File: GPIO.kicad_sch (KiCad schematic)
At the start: 8 parts, among them IC1 ECP5-BGA256, J4 Micro_SD_Card

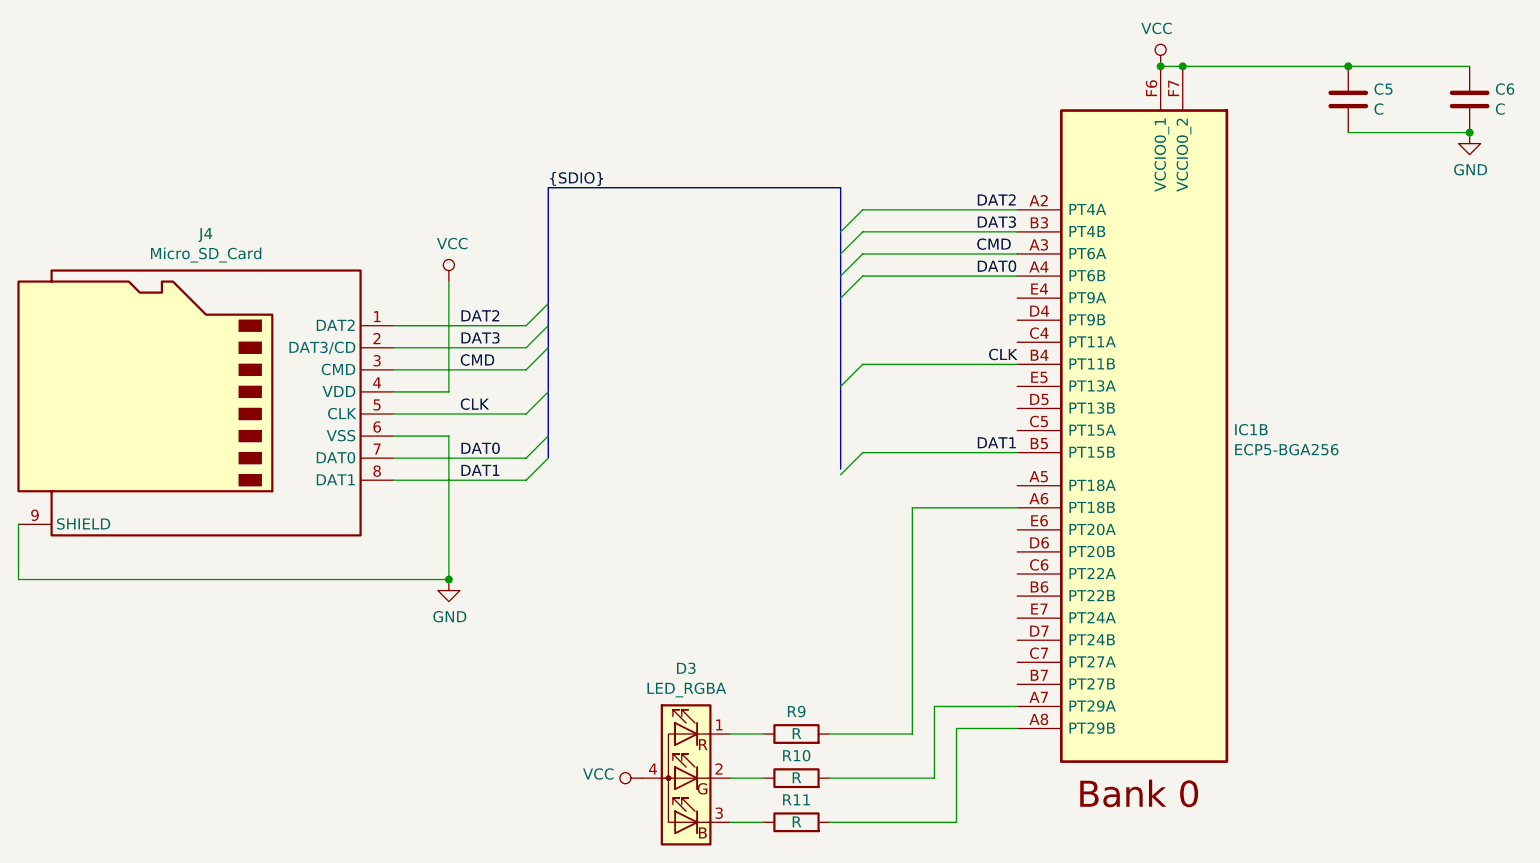
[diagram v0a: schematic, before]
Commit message: Remove SD card, relocate regulators
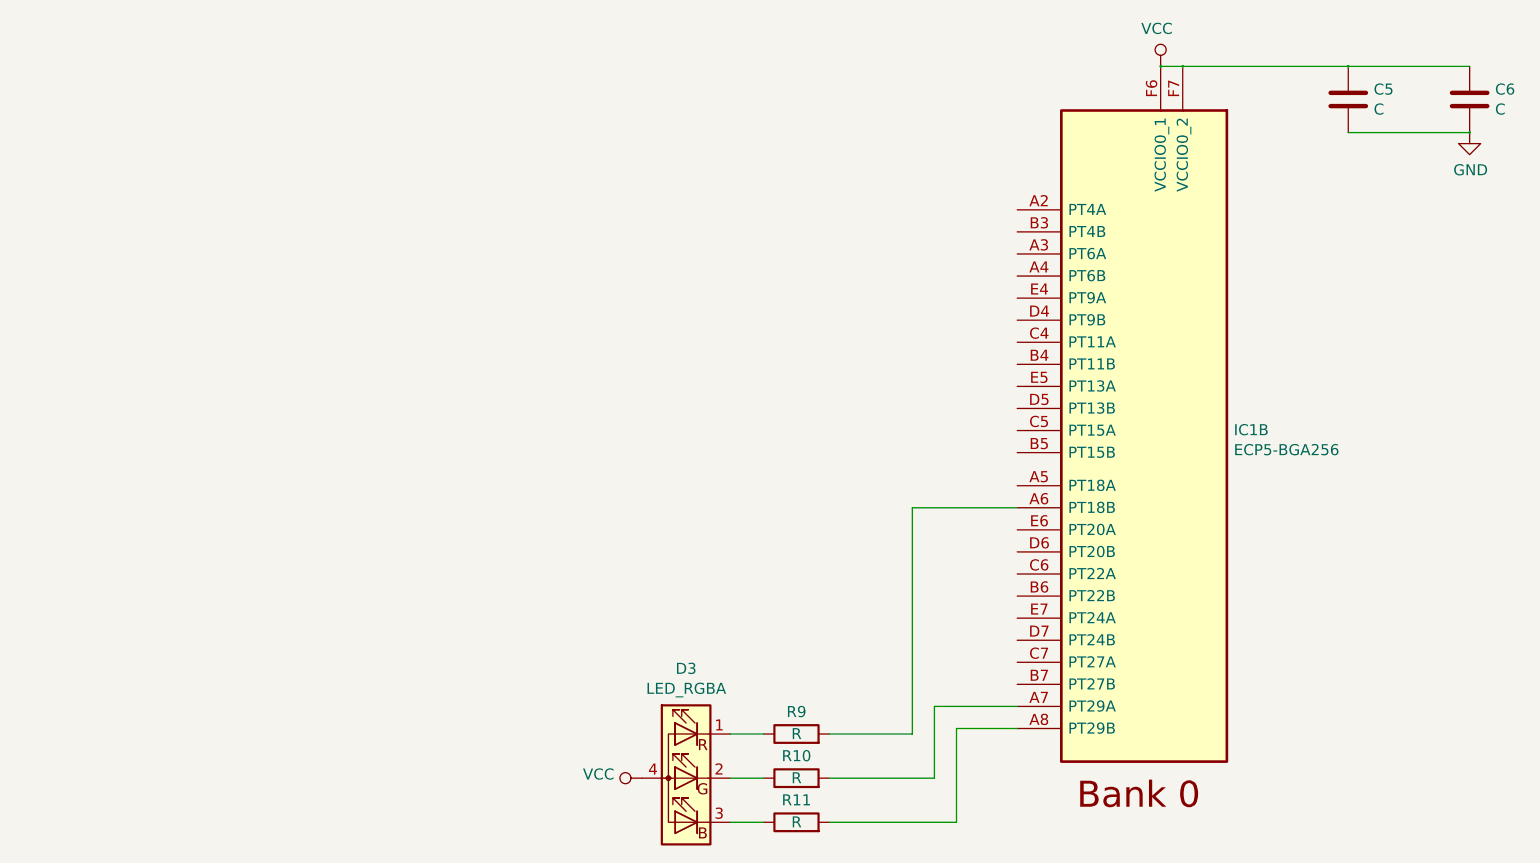
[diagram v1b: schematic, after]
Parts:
- removed J4: Micro_SD_Card, Connector_Card:microSD_HC_Wuerth_693072010801, symbol Connector:Micro_SD_Card
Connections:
- net CLK: no longer names the net of IC1.B4 (PT11B)
- net CMD: no longer names the net of IC1.A3 (PT6A)
- net DAT0: no longer names the net of IC1.A4 (PT6B)
- net DAT1: no longer names the net of IC1.B5 (PT15B)
- net DAT2: no longer names the net of IC1.A2 (PT4A)
- net DAT3: no longer names the net of IC1.B3 (PT4B)
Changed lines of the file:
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@@
-(kicad_sch (version 20200714) (host eeschema "5.99.0-unknown-8324cb3~102~ubuntu20.04.1")
-  (page 1 6)
+(kicad_sch (version 20200714) (host eeschema "5.99.0-unknown-027b6c8cf~102~ubuntu20.04.1")
+  (page 6 6)
   (paper "A4")
   (bus_alias "SDIO" (members "DAT[0..3]" "CMD" "CLK"))
-  (junction (at 138.43 109.22) (diameter 0) (color 0 0 0 0))
-  (junction (at 220.345 50.165) (diameter 0) (color 0 0 0 0))
-  (junction (at 222.885 50.165) (diameter 0) (color 0 0 0 0))
-  (junction (at 241.935 50.165) (diameter 0) (color 0 0 0 0))
-  (junction (at 255.905 57.785) (diameter 0) (color 0 0 0 0))
-  (bus_entry (at 147.32 80.01) (size 2.54 -2.54)
-    (stroke (width 0.1524) (type solid) (color 0 0 0 0))
-  )
-  (bus_entry (at 147.32 82.55) (size 2.54 -2.54)
-    (stroke (width 0.1524) (type solid) (color 0 0 0 0))
-  )
-  (bus_entry (at 147.32 85.09) (size 2.54 -2.54)
-    (stroke (width 0.1524) (type solid) (color 0 0 0 0))
-  )
-  (bus_entry (at 147.32 90.17) (size 2.54 -2.54)
-    (stroke (width 0.1524) (type solid) (color 0 0 0 0))
-  )
-  (bus_entry (at 147.32 95.25) (size 2.54 -2.54)
-    (stroke (width 0.1524) (type solid) (color 0 0 0 0))
-  )
-  (bus_entry (at 147.32 97.79) (size 2.54 -2.54)
-    (stroke (width 0.1524) (type solid) (color 0 0 0 0))
-  )
-  (bus_entry (at 183.515 69.215) (size 2.54 -2.54)
-    (stroke (width 0.1524) (type solid) (color 0 0 0 0))
-  )
-  (bus_entry (at 183.515 71.755) (size 2.54 -2.54)
-    (stroke (width 0.1524) (type solid) (color 0 0 0 0))
-  )
-  (bus_entry (at 183.515 74.295) (size 2.54 -2.54)
-    (stroke (width 0.1524) (type solid) (color 0 0 0 0))
-  )
-  (bus_entry (at 183.515 76.835) (size 2.54 -2.54)
-    (stroke (width 0.1524) (type solid) (color 0 0 0 0))
-  )
-  (bus_entry (at 183.515 86.995) (size 2.54 -2.54)
-    (stroke (width 0.1524) (type solid) (color 0 0 0 0))
-  )
-  (bus_entry (at 183.515 97.155) (size 2.54 -2.54)
-    (stroke (width 0.1524) (type solid) (color 0 0 0 0))
-  )
-  (wire (pts (xy 88.9 102.87) (xy 88.9 109.22))
-    (stroke (width 0) (type solid) (color 0 0 0 0))
-  )
-  (wire (pts (xy 88.9 109.22) (xy 138.43 109.22))
-    (stroke (width 0) (type solid) (color 0 0 0 0))
-  )
-  (wire (pts (xy 132.08 80.01) (xy 147.32 80.01))
-    (stroke (width 0) (type solid) (color 0 0 0 0))
-  )
-  (wire (pts (xy 132.08 82.55) (xy 147.32 82.55))
-    (stroke (width 0) (type solid) (color 0 0 0 0))
-  )
-  (wire (pts (xy 132.08 85.09) (xy 147.32 85.09))
-    (stroke (width 0) (type solid) (color 0 0 0 0))
-  )
-  (wire (pts (xy 132.08 90.17) (xy 147.32 90.17))
-    (stroke (width 0) (type solid) (color 0 0 0 0))
-  )
-  (wire (pts (xy 132.08 92.71) (xy 138.43 92.71))
-    (stroke (width 0) (type solid) (color 0 0 0 0))
-  )
-  (wire (pts (xy 132.08 95.25) (xy 147.32 95.25))
-    (stroke (width 0) (type solid) (color 0 0 0 0))
-  )
-  (wire (pts (xy 132.08 97.79) (xy 147.32 97.79))
-    (stroke (width 0) (type solid) (color 0 0 0 0))
-  )
-  (wire (pts (xy 138.43 74.93) (xy 138.43 87.63))
-    (stroke (width 0) (type solid) (color 0 0 0 0))
-  )
-  (wire (pts (xy 138.43 87.63) (xy 132.08 87.63))
-    (stroke (width 0) (type solid) (color 0 0 0 0))
-  )
-  (wire (pts (xy 138.43 92.71) (xy 138.43 109.22))
-    (stroke (width 0) (type solid) (color 0 0 0 0))
-  )
+  (junction (at 220.345 50.165) (diameter 0.3048) (color 0 0 0 0))
+  (junction (at 222.885 50.165) (diameter 0.3048) (color 0 0 0 0))
+  (junction (at 241.935 50.165) (diameter 0.3048) (color 0 0 0 0))
+  (junction (at 255.905 57.785) (diameter 0.3048) (color 0 0 0 0))
   (wire (pts (xy 170.815 127) (xy 174.625 127))
     (stroke (width 0) (type solid) (color 0 0 0 0))
@@
   )
   (wire (pts (xy 182.245 132.08) (xy 194.31 132.08))
-    (stroke (width 0) (type solid) (color 0 0 0 0))
-  )
-  (wire (pts (xy 186.055 66.675) (xy 203.835 66.675))
-    (stroke (width 0) (type solid) (color 0 0 0 0))
-  )
-  (wire (pts (xy 186.055 69.215) (xy 203.835 69.215))
-    (stroke (width 0) (type solid) (color 0 0 0 0))
-  )
-  (wire (pts (xy 186.055 71.755) (xy 203.835 71.755))
-    (stroke (width 0) (type solid) (color 0 0 0 0))
-  )
-  (wire (pts (xy 186.055 74.295) (xy 203.835 74.295))
-    (stroke (width 0) (type solid) (color 0 0 0 0))
-  )
-  (wire (pts (xy 186.055 84.455) (xy 203.835 84.455))
-    (stroke (width 0) (type solid) (color 0 0 0 0))
-  )
-  (wire (pts (xy 186.055 94.615) (xy 203.835 94.615))
     (stroke (width 0) (type solid) (color 0 0 0 0))
   )
@@
     (stroke (width 0) (type solid) (color 0 0 0 0))
   )
-  (bus (pts (xy 149.86 64.135) (xy 149.86 80.01))
-    (stroke (width 0) (type solid) (color 0 0 0 0))
-  )
-  (bus (pts (xy 149.86 80.01) (xy 149.86 82.55))
-    (stroke (width 0) (type solid) (color 0 0 0 0))
-  )
-  (bus (pts (xy 149.86 82.55) (xy 149.86 92.71))
-    (stroke (width 0) (type solid) (color 0 0 0 0))
-  )
-  (bus (pts (xy 149.86 92.71) (xy 149.86 95.25))
-    (stroke (width 0) (type solid) (color 0 0 0 0))
-  )
-  (bus (pts (xy 183.515 64.135) (xy 149.86 64.135))
-    (stroke (width 0) (type solid) (color 0 0 0 0))
-  )
-  (bus (pts (xy 183.515 64.135) (xy 183.515 69.215))
-    (stroke (width 0) (type solid) (color 0 0 0 0))
-  )
-  (bus (pts (xy 183.515 69.215) (xy 183.515 74.295))
-    (stroke (width 0) (type solid) (color 0 0 0 0))
-  )
-  (bus (pts (xy 183.515 74.295) (xy 183.515 86.995))
-    (stroke (width 0) (type solid) (color 0 0 0 0))
-  )
-  (bus (pts (xy 183.515 86.995) (xy 183.515 96.52))
-    (stroke (width 0) (type solid) (color 0 0 0 0))
-  )
-  (label "DAT2" (at 139.7 80.01 0)
-    (effects (font (size 1.27 1.27)) (justify left bottom))
-  )
-  (label "DAT3" (at 139.7 82.55 0)
-    (effects (font (size 1.27 1.27)) (justify left bottom))
-  )
-  (label "CMD" (at 139.7 85.09 0)
-    (effects (font (size 1.27 1.27)) (justify left bottom))
-  )
-  (label "CLK" (at 139.7 90.17 0)
-    (effects (font (size 1.27 1.27)) (justify left bottom))
-  )
-  (label "DAT0" (at 139.7 95.25 0)
-    (effects (font (size 1.27 1.27)) (justify left bottom))
-  )
-  (label "DAT1" (at 139.7 97.79 0)
-    (effects (font (size 1.27 1.27)) (justify left bottom))
-  )
-  (label "{SDIO}" (at 149.86 64.135 0)
-    (effects (font (size 1.27 1.27)) (justify left bottom))
-  )
-  (label "CMD" (at 203.2 71.755 180)
-    (effects (font (size 1.27 1.27)) (justify right bottom))
-  )
-  (label "DAT2" (at 203.835 66.675 180)
-    (effects (font (size 1.27 1.27)) (justify right bottom))
-  )
-  (label "DAT3" (at 203.835 69.215 180)
-    (effects (font (size 1.27 1.27)) (justify right bottom))
-  )
-  (label "DAT0" (at 203.835 74.295 180)
-    (effects (font (size 1.27 1.27)) (justify right bottom))
-  )
-  (label "CLK" (at 203.835 84.455 180)
-    (effects (font (size 1.27 1.27)) (justify right bottom))
-  )
-  (label "DAT1" (at 203.835 94.615 180)
-    (effects (font (size 1.27 1.27)) (justify right bottom))
-  )
-  (symbol (lib_id "power:VCC") (at 138.43 74.93 0) (unit 1)
-    (in_bom yes) (on_board yes)
-    (property "Reference" "#PWR0145" (id 0) (at 138.43 78.74 0)
-      (effects (font (size 1.27 1.27)) hide)
-    )
-    (property "Value" "VCC" (id 1) (at 138.8618 70.6056 0))
-    (property "Footprint" "" (id 2) (at 138.43 74.93 0)
-      (effects (font (size 1.27 1.27)) hide)
-    )
-    (property "Datasheet" "" (id 3) (at 138.43 74.93 0)
-      (effects (font (size 1.27 1.27)) hide)
-    )
-  )
   (symbol (lib_id "power:VCC") (at 160.655 132.08 90) (unit 1)
     (in_bom yes) (on_board yes)
@@
     )
     (property "Datasheet" "" (id 3) (at 220.345 50.165 0)
-      (effects (font (size 1.27 1.27)) hide)
-    )
-  )
-  (symbol (lib_id "power:GND") (at 138.43 109.22 0) (unit 1)
-    (in_bom yes) (on_board yes)
-    (property "Reference" "#PWR0144" (id 0) (at 138.43 115.57 0)
-      (effects (font (size 1.27 1.27)) hide)
-    )
-    (property "Value" "GND" (id 1) (at 138.5443 113.5444 0))
-    (property "Footprint" "" (id 2) (at 138.43 109.22 0)
-      (effects (font (size 1.27 1.27)) hide)
-    )
-    (property "Datasheet" "" (id 3) (at 138.43 109.22 0)
       (effects (font (size 1.27 1.27)) hide)
     )
@@
       (effects (font (size 1.27 1.27)) hide)
     )
-  )
-  (symbol (lib_id "Connector:Micro_SD_Card") (at 109.22 87.63 0) (mirror y) (unit 1)
-    (in_bom yes) (on_board yes)
-    (property "Reference" "J4" (id 0) (at 110.49 69.4498 0))
-    (property "Value" "Micro_SD_Card" (id 1) (at 110.49 71.7485 0))
-    (property "Footprint" "Connector_Card:microSD_HC_Wuerth_693072010801" (id 2) (at 80.01 80.01 0)
-      (effects (font (size 1.27 1.27)) hide)
-    )
-    (property "Datasheet" "http://katalog.we-online.de/em/datasheet/693072010801.pdf" (id 3) (at 109.22 87.63 0)
-      (effects (font (size 1.27 1.27)) hide)
-    )
